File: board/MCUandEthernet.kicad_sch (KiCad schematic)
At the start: 3 parts, among them J1 RJ45_LED_Shielded, U15 Teensy4.1_DEV-16771

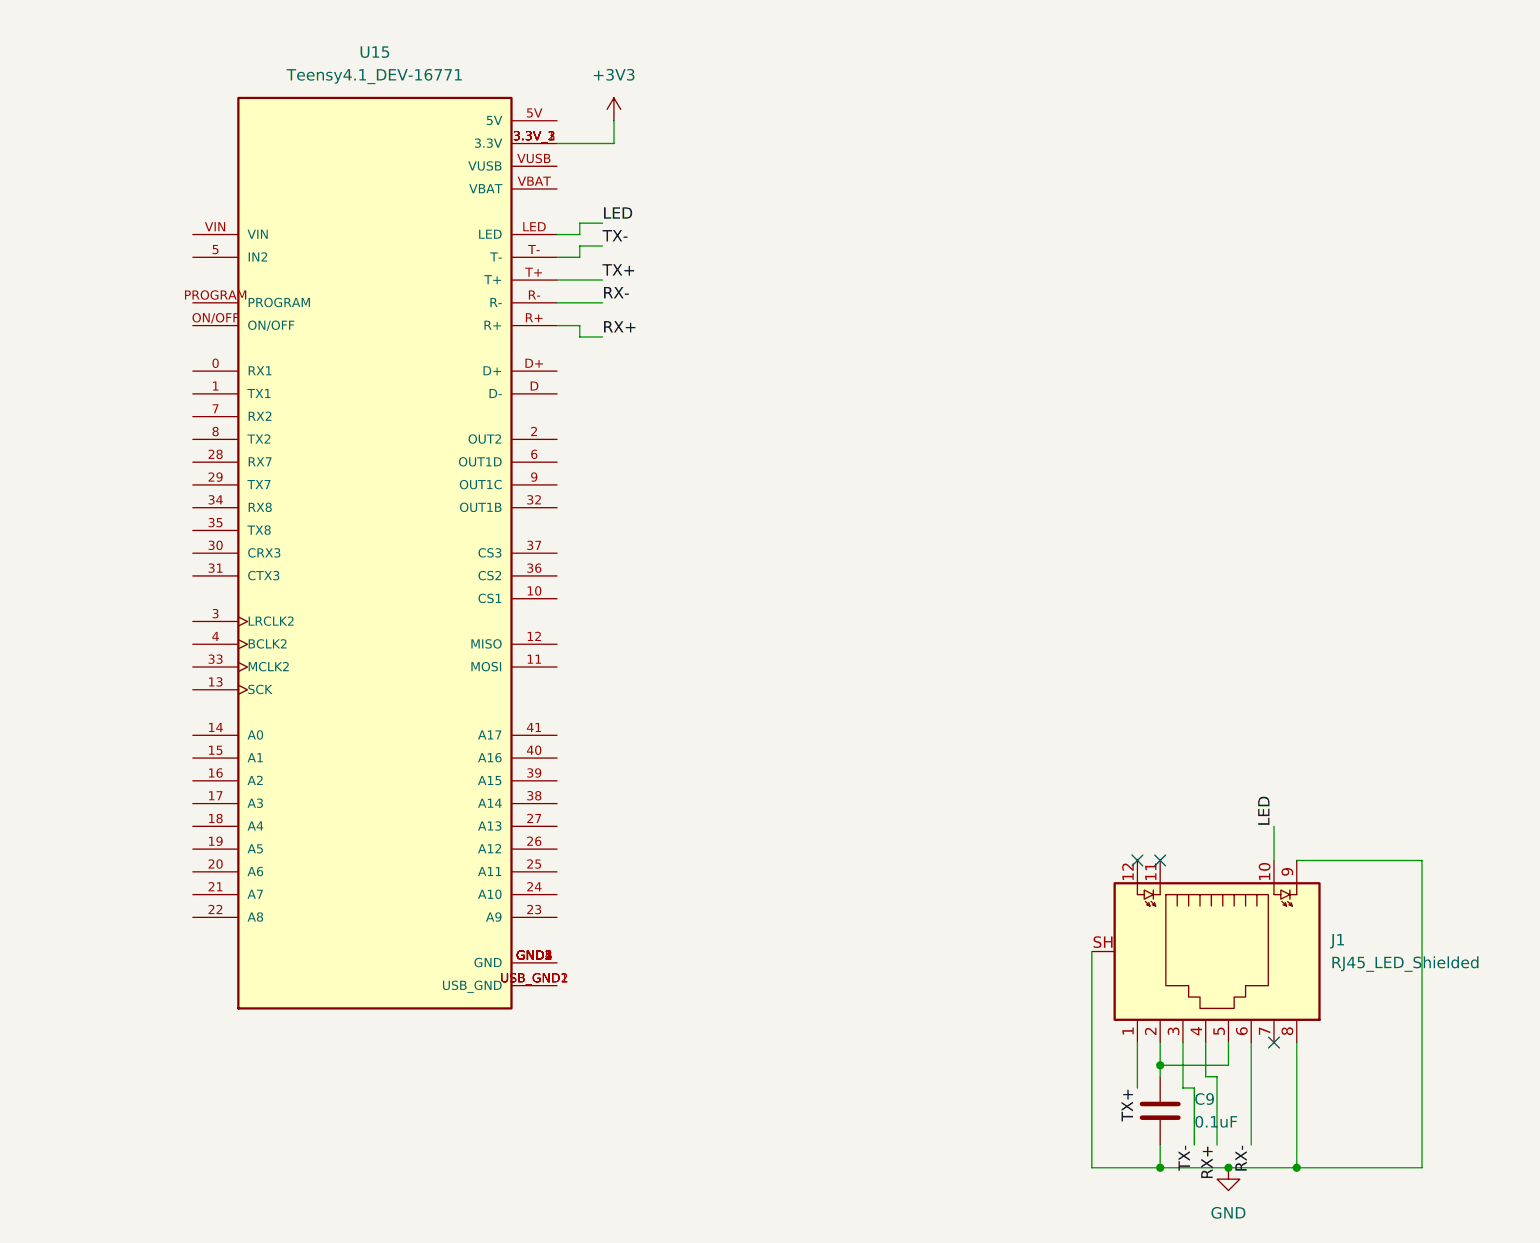
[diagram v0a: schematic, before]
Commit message: added current sense flags to teensy
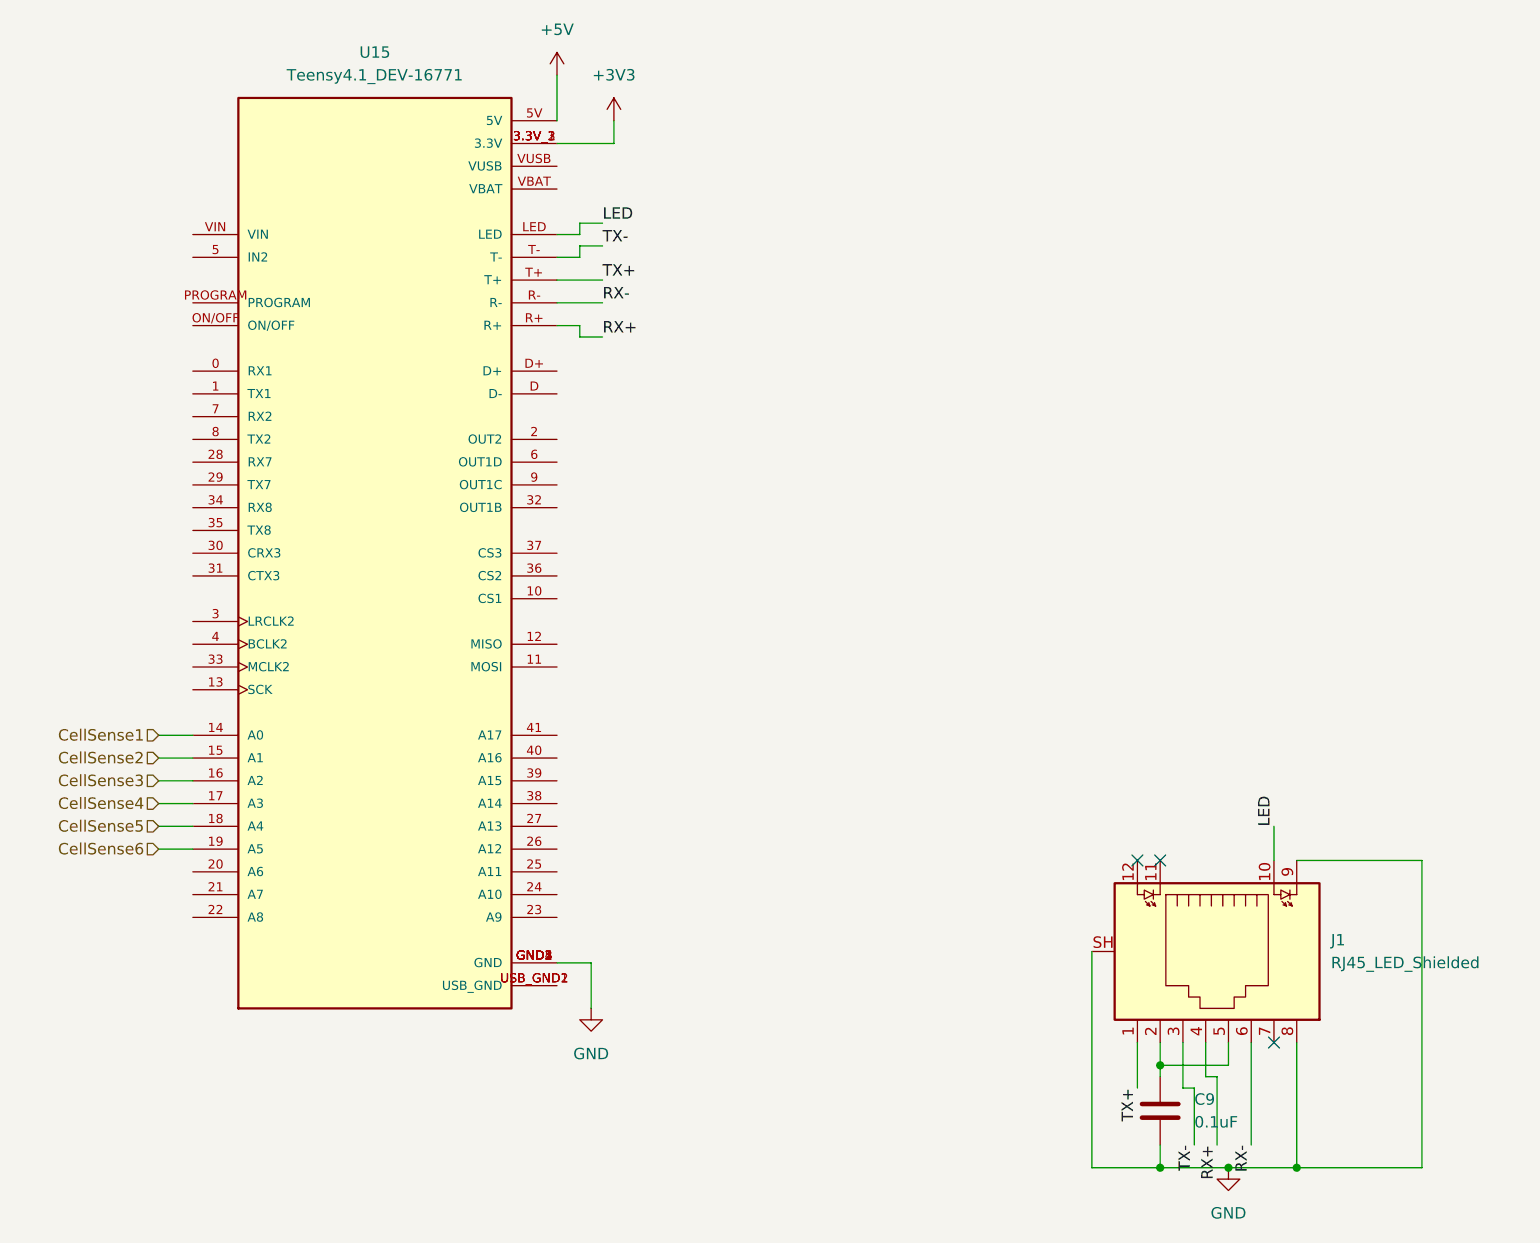
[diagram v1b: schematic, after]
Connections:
- net GND: now also U15.GND1 (GND), U15.GND2 (GND), U15.GND3 (GND), U15.GND4 (GND), U15.GND5 (GND)
- net CellSense1: now reaches U15.14 (A0)
- net CellSense2: now reaches U15.15 (A1)
- net CellSense3: now reaches U15.16 (A2)
- net CellSense4: now reaches U15.17 (A3)
- net CellSense5: now reaches U15.18 (A4)
- net CellSense6: now reaches U15.19 (A5)
- net +5V: now reaches U15.5V

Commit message: Added MCU Flags
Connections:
- net GND: now also U15.USB_GND1 (USB_GND), U15.USB_GND2 (USB_GND)
- net BuzzerSignal: now reaches U15.39 (A15)
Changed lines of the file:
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@@
+	)
+	(junction
+		(at 72.39 142.24)
+		(diameter 0)
+		(color 0 0 0 0)
 	)
 	(junction
@@
 	(wire
 		(pts
-			(xy 72.39 144.78) (xy 72.39 139.7)
+			(xy 72.39 144.78) (xy 72.39 142.24)
 		)
 		(stroke
@@
 	(wire
 		(pts
+			(xy 68.58 119.38) (xy 73.66 119.38)
+		)
+		(stroke
+			(width 0)
+			(type default)
+		)
+	)
+	(wire
+		(pts
 			(xy 138.43 153.67) (xy 138.43 148.59)
 		)
@@
 		(pts
 			(xy 135.89 151.13) (xy 143.51 151.13)
+		)
+		(stroke
+			(width 0)
+			(type default)
+		)
+	)
+	(wire
+		(pts
+			(xy 68.58 142.24) (xy 72.39 142.24)
+		)
+		(stroke
+			(width 0)
+			(type default)
+		)
+	)
+	(wire
+		(pts
+			(xy 72.39 142.24) (xy 72.39 139.7)
 		)
 		(stroke
@@
 		)
 	)
+	(hierarchical_label "BuzzerSignal"
+		(shape output)
+		(at 73.66 119.38 0)
+		(effects
+			(font
+				(size 1.27 1.27)
+			)
+			(justify left)
+		)
+	)

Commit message: add mosfett and teensy switch pins
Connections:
- net NS_Enable: now reaches U15.2 (OUT2)
- net Motor_Enable: now reaches U15.32 (OUT1B)
- net LC_Enable: now reaches U15.37 (CS3)
- net AUX_Enable: now reaches U15.6 (OUT1D)
- net POE_Enable: now reaches U15.9 (OUT1C)
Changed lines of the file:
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@@
+	(wire
+		(pts
+			(xy 68.58 86.36) (xy 71.12 86.36)
+		)
+		(stroke
+			(width 0)
+			(type default)
+		)
+	)
 	(wire
 		(pts
@@
 	(wire
 		(pts
+			(xy 68.58 88.9) (xy 71.12 88.9)
+		)
+		(stroke
+			(width 0)
+			(type default)
+		)
+	)
+	(wire
+		(pts
+			(xy 68.58 83.82) (xy 71.12 83.82)
+		)
+		(stroke
+			(width 0)
+			(type default)
+		)
+	)
+	(wire
+		(pts
 			(xy 73.66 59.69) (xy 71.12 59.69)
 		)
@@
 	(wire
 		(pts
+			(xy 71.12 93.98) (xy 68.58 93.98)
+		)
+		(stroke
+			(width 0)
+			(type default)
+		)
+	)
+	(wire
+		(pts
 			(xy 71.12 69.85) (xy 71.12 68.58)
 		)
@@
 		(pts
 			(xy 24.13 121.92) (xy 27.94 121.92)
+		)
+		(stroke
+			(width 0)
+			(type default)
+		)
+	)
+	(wire
+		(pts
+			(xy 71.12 81.28) (xy 68.58 81.28)
 		)
 		(stroke
@@
 		)
 	)
+	(hierarchical_label "Motor_Enable"
+		(shape output)
+		(at 71.12 88.9 0)
+		(effects
+			(font
+				(size 1.27 1.27)
+			)
+			(justify left)
+		)
+	)
 	(hierarchical_label "CellSense2"
 		(shape input)
@@
 		)
 	)
+	(hierarchical_label "AUX_Enable"
+		(shape output)
+		(at 71.12 83.82 0)
+		(effects
+			(font
+				(size 1.27 1.27)
+			)
+			(justify left)
+		)
+	)
+	(hierarchical_label "LC_Enable"
+		(shape output)
+		(at 71.12 93.98 0)
+		(effects
+			(font
+				(size 1.27 1.27)
+			)
+			(justify left)
+		)
+	)
+	(hierarchical_label "NS_Enable"
+		(shape output)
+		(at 71.12 81.28 0)
+		(effects
+			(font
+				(size 1.27 1.27)
+			)
+			(justify left)
+		)
+	)
+	(hierarchical_label "POE_Enable"
+		(shape output)
+		(at 71.12 86.36 0)
+		(effects
+			(font
+				(size 1.27 1.27)
+			)
+			(justify left)
+		)
+	)

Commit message: Current Sensors FABRICATED
Current Sensor Hierarchy sheet created
Contains:
- Network Switch current sensing
- POE current sensing
- Low Current current sensing
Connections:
- net CSenseLC: now reaches U15.20 (A6)
- net CSenseNS: now reaches U15.21 (A7)
- net CSensePOE: now reaches U15.22 (A8)
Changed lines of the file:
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@@
+	(wire
+		(pts
+			(xy 24.13 134.62) (xy 27.94 134.62)
+		)
+		(stroke
+			(width 0)
+			(type default)
+		)
+	)
 	(wire
 		(pts
@@
 	(wire
 		(pts
+			(xy 24.13 129.54) (xy 27.94 129.54)
+		)
+		(stroke
+			(width 0)
+			(type default)
+		)
+	)
+	(wire
+		(pts
 			(xy 73.66 69.85) (xy 71.12 69.85)
 		)
@@
 		(pts
 			(xy 68.58 66.04) (xy 73.66 66.04)
+		)
+		(stroke
+			(width 0)
+			(type default)
+		)
+	)
+	(wire
+		(pts
+			(xy 24.13 132.08) (xy 27.94 132.08)
 		)
 		(stroke
@@
 			)
 			(justify left bottom)
+		)
+	)
+	(hierarchical_label "CSensePOE"
+		(shape input)
+		(at 24.13 134.62 180)
+		(effects
+			(font
+				(size 1.27 1.27)
+			)
+			(justify right)
 		)
 	)
@@
 		(effects
 			(font
+				(size 1.27 1.27)
+			)
+			(justify right)
+		)
+	)
+	(hierarchical_label "CSenseLC"
+		(shape input)
+		(at 24.13 129.54 180)
+		(effects
+			(font
+				(size 1.27 1.27)
+			)
+			(justify right)
+		)
+	)
+	(hierarchical_label "CSenseNS"
+		(shape input)
+		(at 24.13 132.08 180)
+		(effects
+			(font

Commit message: BattCSense added
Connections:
- net CSenseBatt: now reaches U15.41 (A17)
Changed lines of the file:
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@@
+	(wire
+		(pts
+			(xy 68.58 114.3) (xy 73.66 114.3)
+		)
+		(stroke
+			(width 0)
+			(type default)
+		)
+	)
 	(wire
 		(pts
@@
 		(effects
 			(font
+				(size 1.27 1.27)
+			)
+			(justify left)
+		)
+	)
+	(hierarchical_label "CSenseBatt"
+		(shape input)
+		(at 73.66 114.3 0)
+		(effects
+			(font

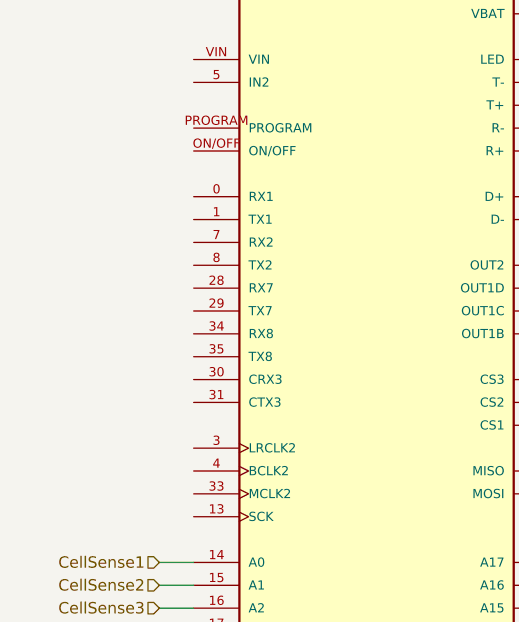
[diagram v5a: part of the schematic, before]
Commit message: Added LCD
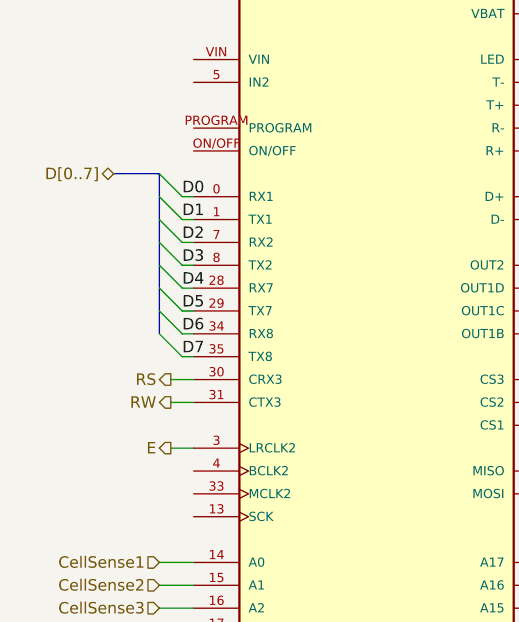
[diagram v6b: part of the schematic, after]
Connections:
- net D0: now reaches U15.0 (RX1)
- net D1: now reaches U15.1 (TX1)
- net D4: now reaches U15.28 (RX7)
- net D5: now reaches U15.29 (TX7)
- net E: now reaches U15.3 (LRCLK2)
- net RS: now reaches U15.30 (CRX3)
- net RW: now reaches U15.31 (CTX3)
- net D6: now reaches U15.34 (RX8)
- net D7: now reaches U15.35 (TX8)
- net D2: now reaches U15.7 (RX2)
- net D3: now reaches U15.8 (TX2)

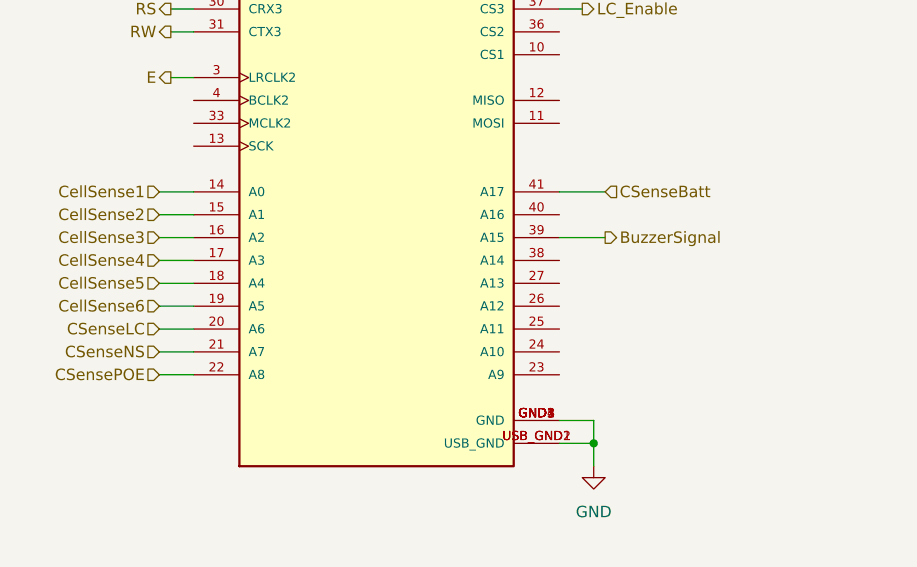
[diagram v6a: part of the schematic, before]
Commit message: Connect Current Sensing Pins
-Connected pins from Switching Circuits, POE, Andersons, Teensy, and Current-Sensinator
-A little organization courtesy of Emilio Baeza
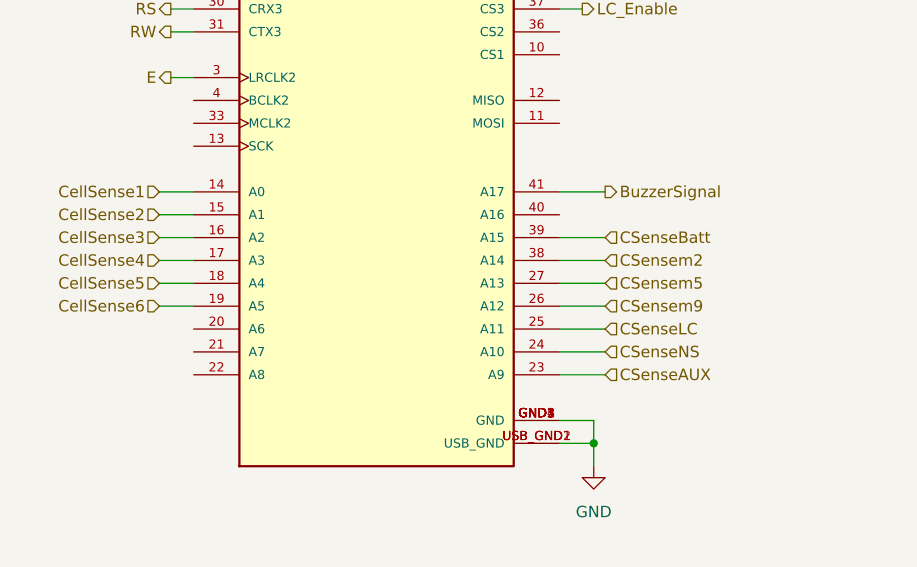
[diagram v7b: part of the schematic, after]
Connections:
- net BuzzerSignal: now also U15.41 (A17); no longer U15.39 (A15)
- net CSenseBatt: now also U15.39 (A15); no longer U15.41 (A17)
- net CSenseLC: now also U15.25 (A11); no longer U15.20 (A6)
- net CSenseNS: now also U15.24 (A10); no longer U15.21 (A7)
- net CSenseAUX: now reaches U15.23 (A9)
- net CSensem9: now reaches U15.26 (A12)
- net CSensem5: now reaches U15.27 (A13)
- net CSensem2: now reaches U15.38 (A14)
- net CSensePOE: no longer names the net of U15.22 (A8)
